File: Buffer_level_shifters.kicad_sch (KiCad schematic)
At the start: 5 parts, among them U1 74LS245, U2 74LS245, U3 74LS245, U4 74LS245, U5 74LS245

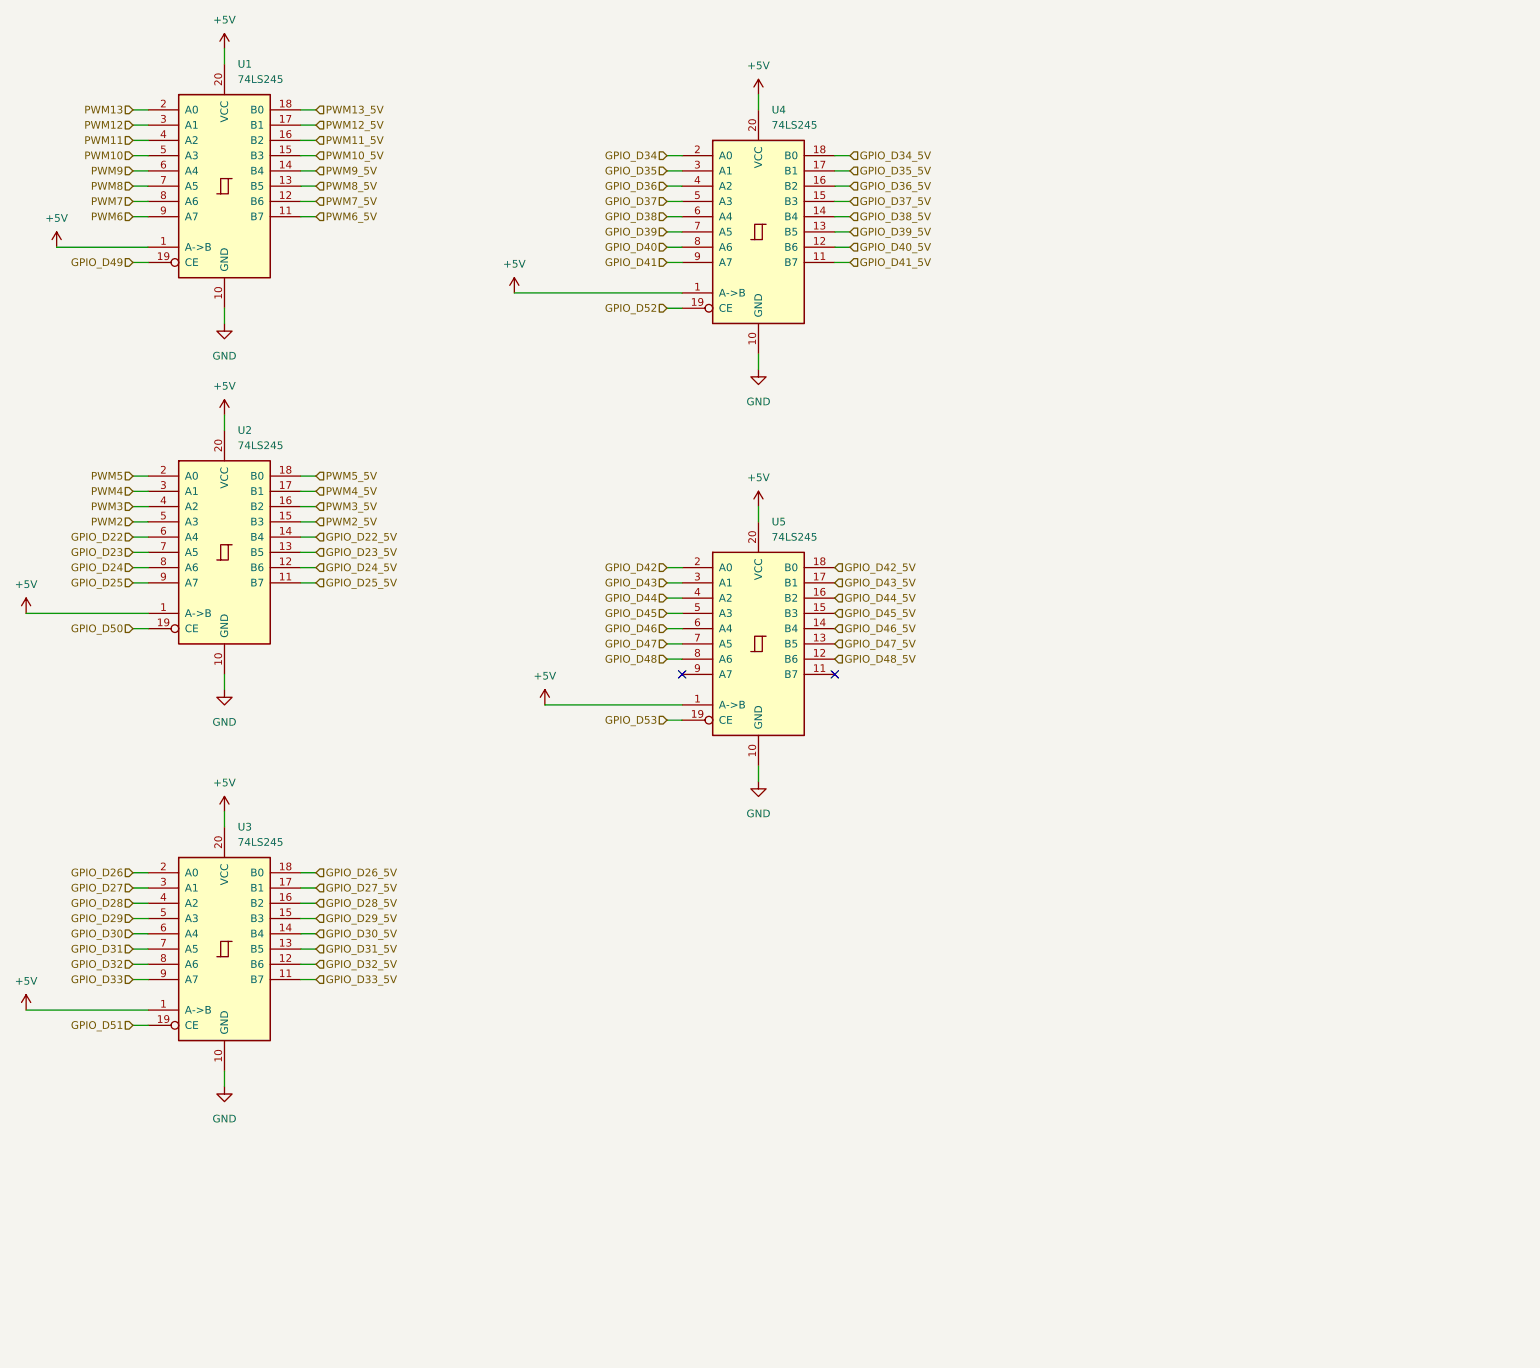
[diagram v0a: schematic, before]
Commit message: PCB REV 001 design
The design of the first revition of the PCB is complete.
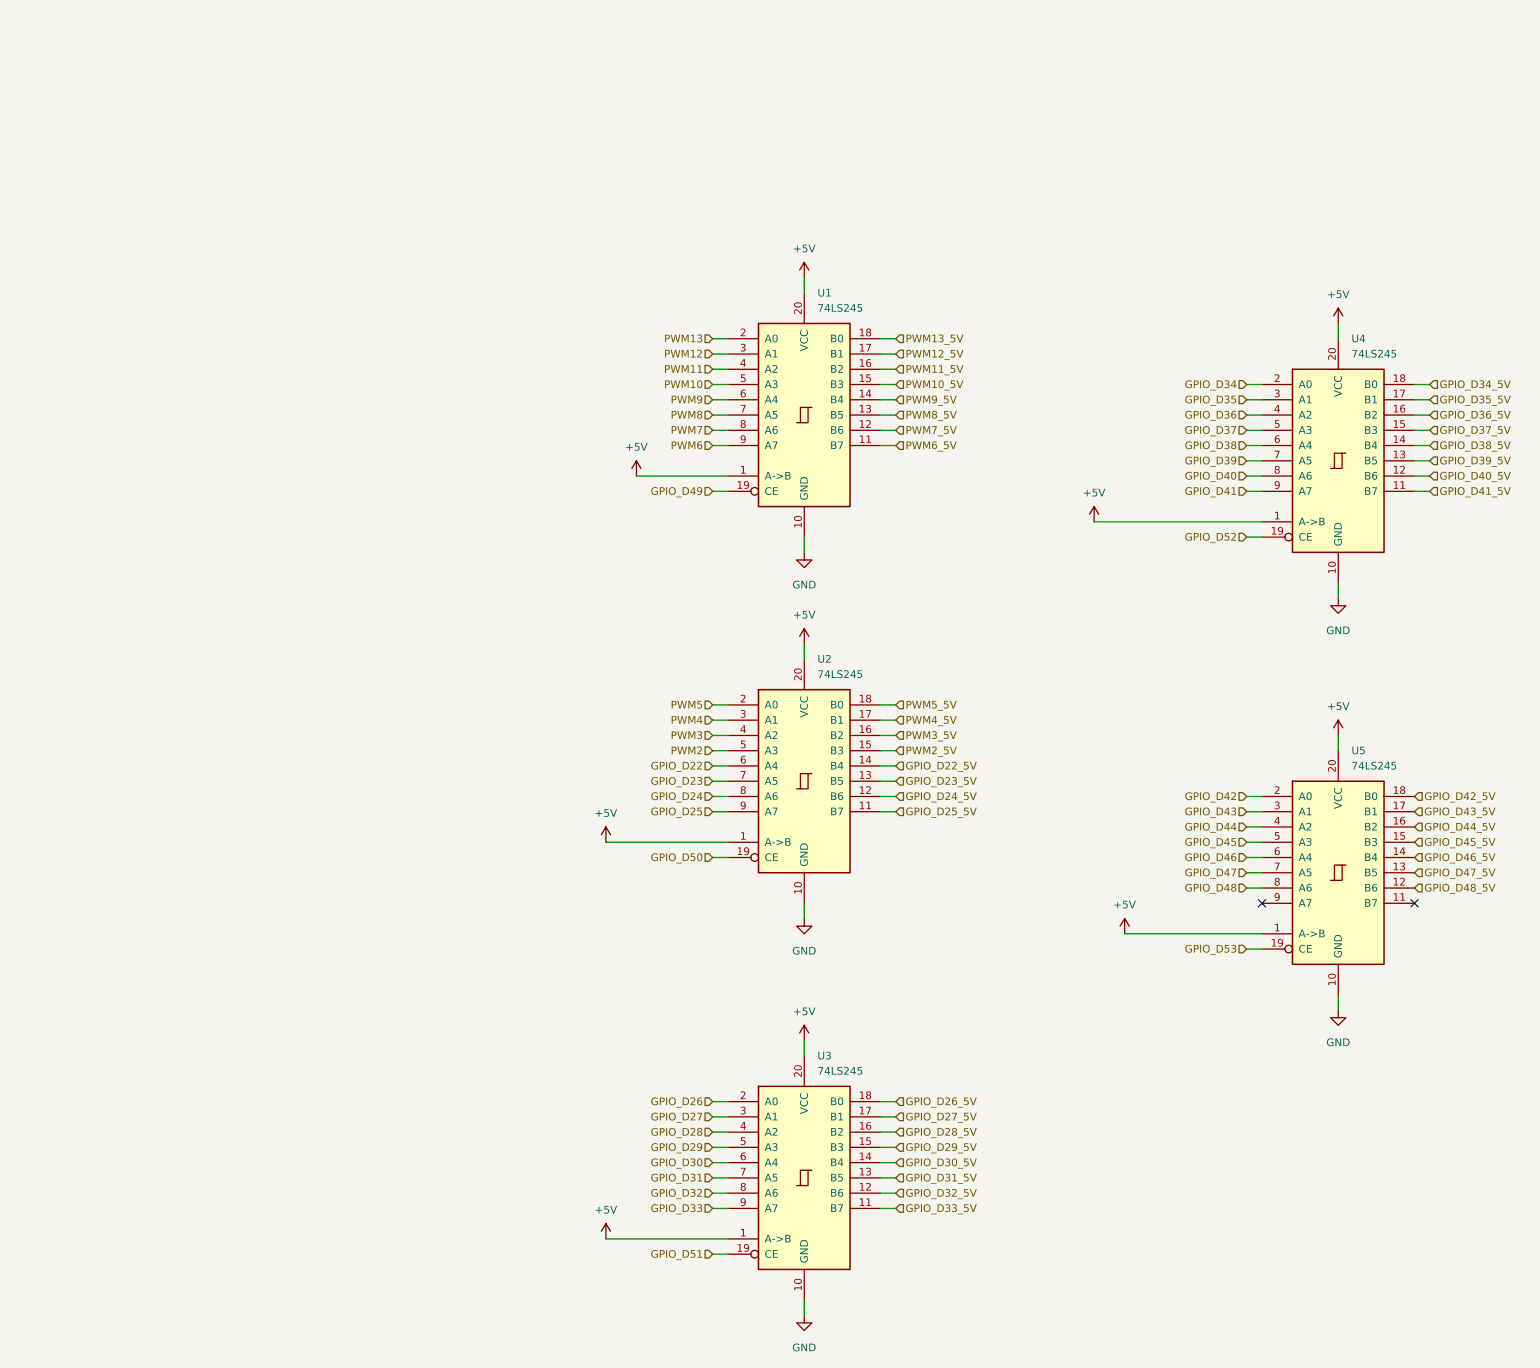
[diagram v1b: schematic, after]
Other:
- moved on the sheet: U1, U2, U3, U4, U5
